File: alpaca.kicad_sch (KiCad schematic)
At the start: 83 parts, among them P1 Debug, P2 Endpoint, U1 Raspberry_Pico, U10 ST_LSM6, U12 ST_LSM6, U2 Alpsalpine_RKJXV, U3 Alpsalpine_EC10E, U4 Alpsalpine_RKJXM, U6 NXP_PCAL6416A, U8 NXP_PCAL6416A

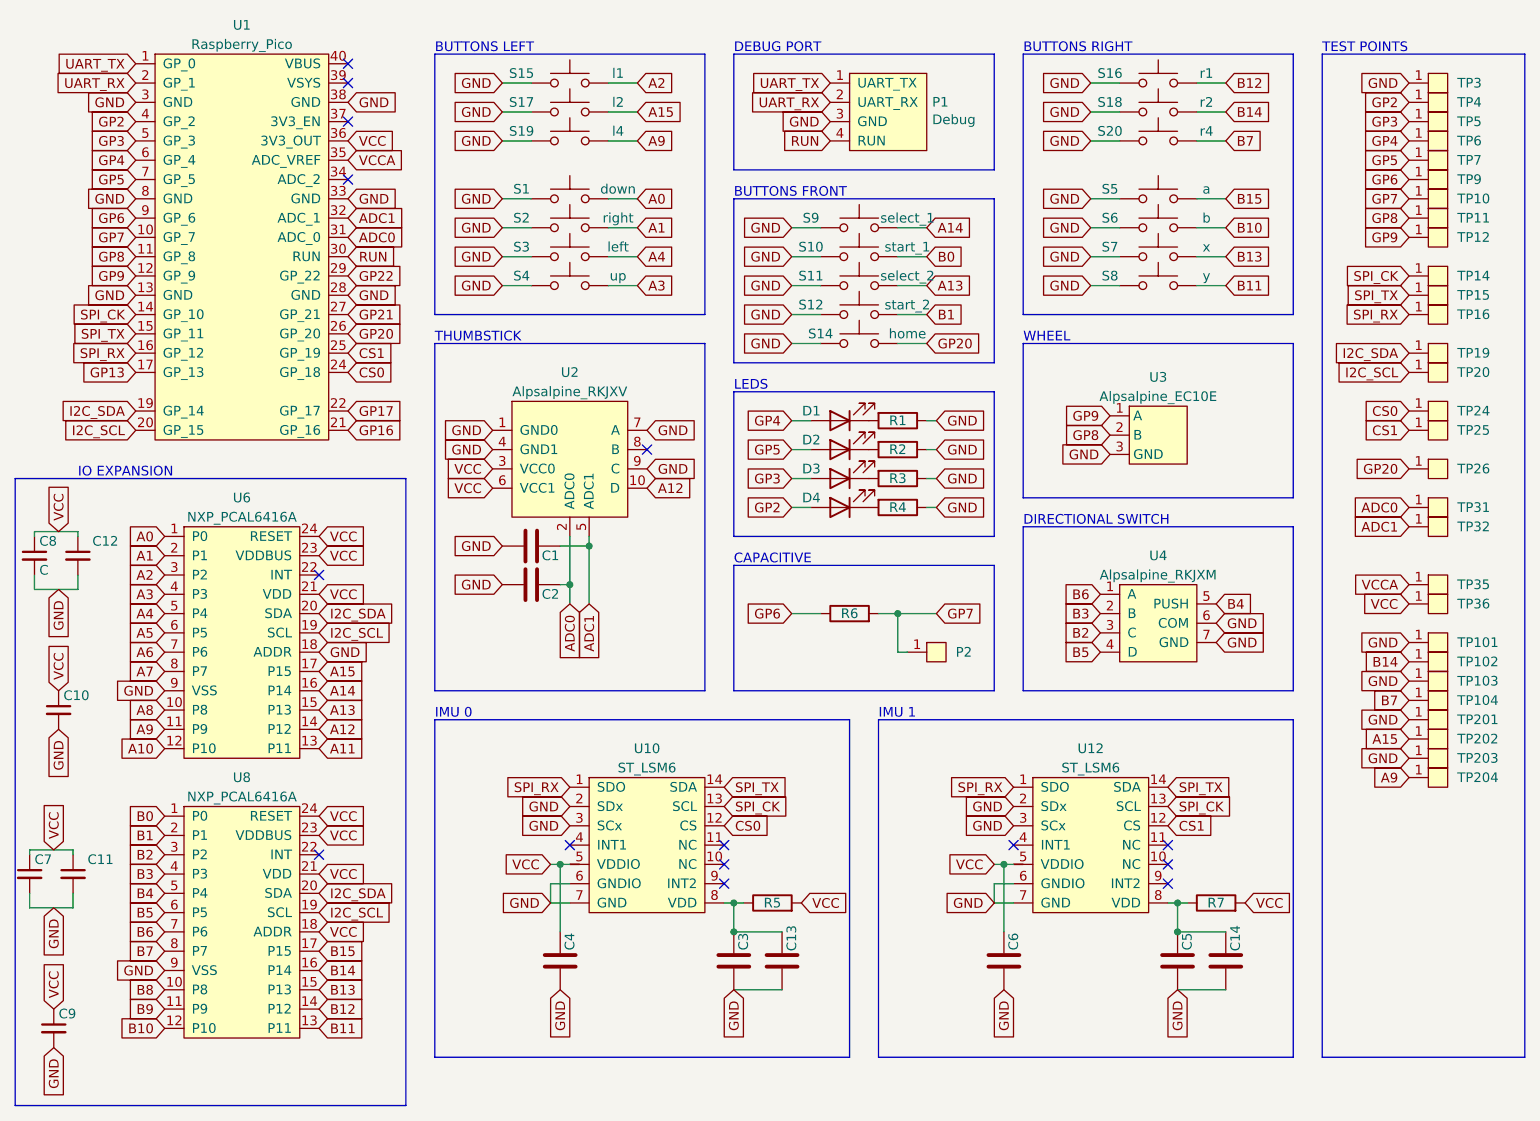
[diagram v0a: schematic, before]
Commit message: Adding hierarchical sheets and bus definitions
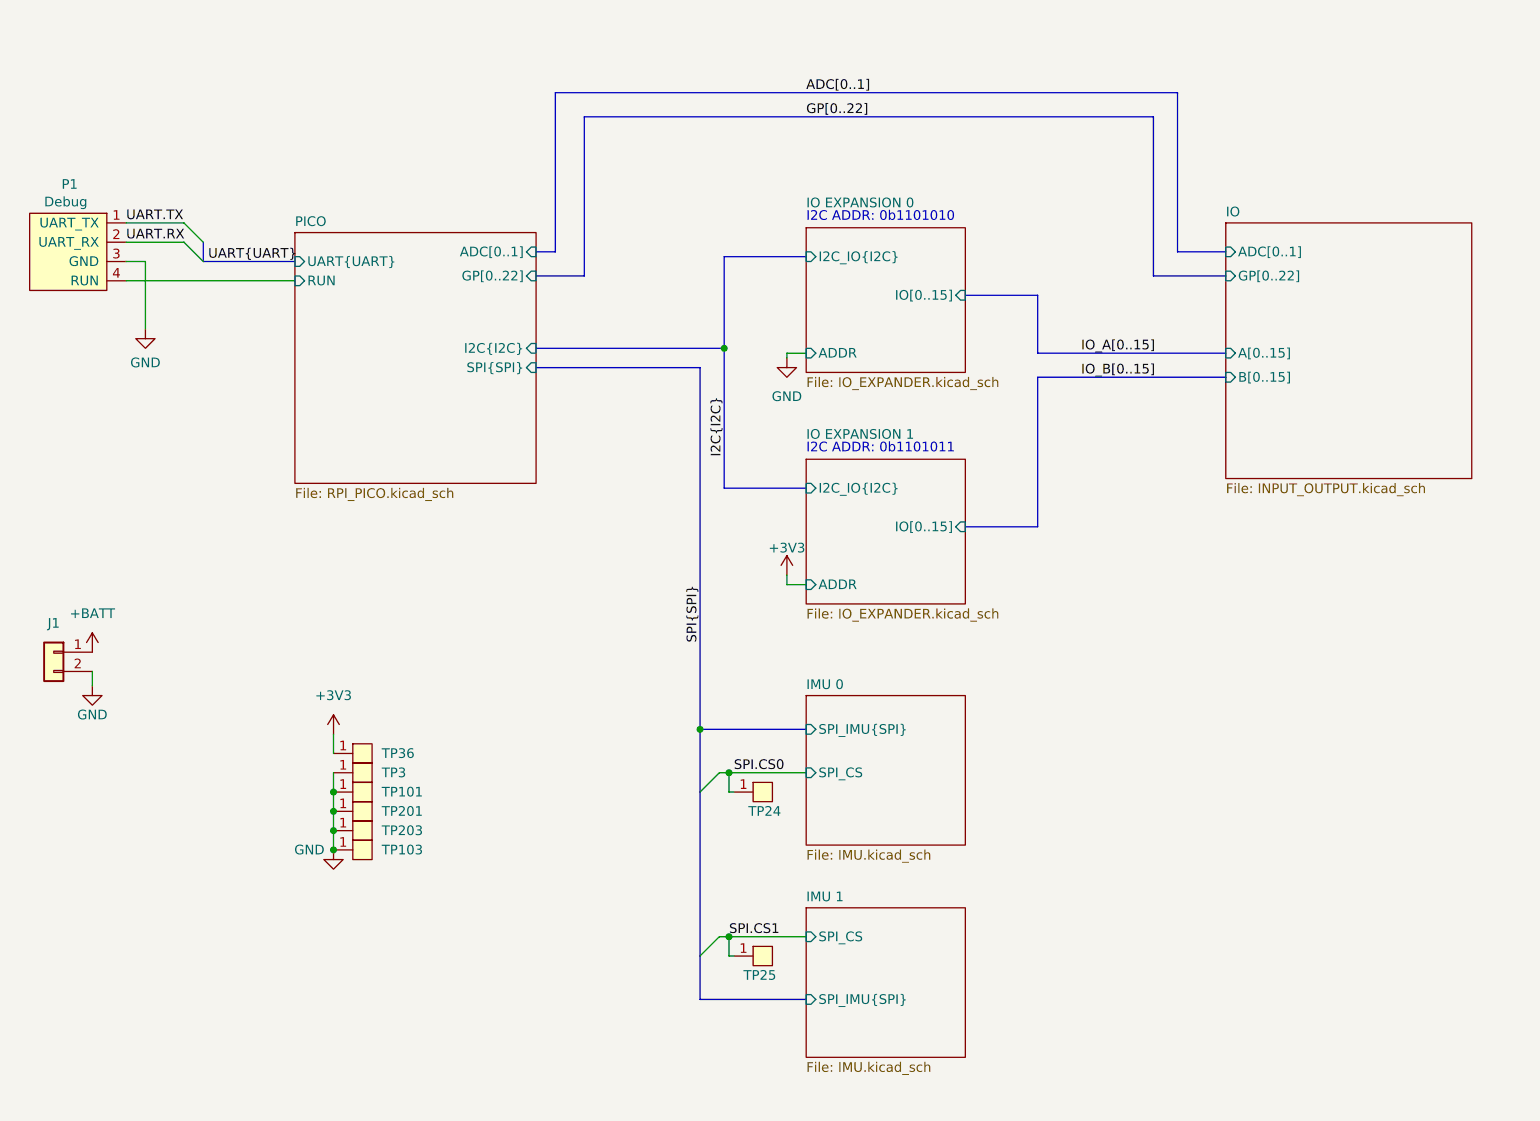
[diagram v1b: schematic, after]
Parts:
- removed C1, C2, C3, C4, C5, C6: C, Capacitor_SMD:C_0402_1005Metric, symbol Device:C
- removed C10, C9: C, Capacitor_SMD:C_0603_1608Metric, symbol Device:C_Small
- removed C11, C12: C, Capacitor_SMD:C_0805_2012Metric, symbol Device:C_Small
- removed C13, C14: C, Capacitor_SMD:C_0603_1608Metric, symbol Device:C
- removed C7, C8: C, Capacitor_SMD:C_0402_1005Metric, symbol Device:C_Small
- removed D1, D2, D3, D4: Diode, ILO_fp:0603_d, symbol Device:LED
- removed P2: Endpoint, ILO_fp:HRO_BC-25-3P, symbol ILO_sym:Endpoint
- removed R1, R2, R3, R4, R5, R7: R, ILO_fp:0603, symbol Device:R
- removed R6: R6, ILO_fp:0402, symbol Device:R
- removed S1: down, ILO_fp:Alpsalpine_SKPM, symbol Switch:SW_Push
- removed S10: start_1, ILO_fp:Alpsalpine_SKPM, symbol Switch:SW_Push
- removed S11: select_2, ILO_fp:Alpsalpine_SKPM, symbol Switch:SW_Push
- removed S12: start_2, ILO_fp:Alpsalpine_SKPM, symbol Switch:SW_Push
- removed S14: home, ILO_fp:Alpsalpine_SKPM, symbol Switch:SW_Push
- removed S15: l1, ILO_fp:Alpsalpine_SKHHL, symbol Switch:SW_Push
- removed S16: r1, ILO_fp:Alpsalpine_SKHHL, symbol Switch:SW_Push
- removed S17: l2, ILO_fp:Alpsalpine_SKQG, symbol Switch:SW_Push
- removed S18: r2, ILO_fp:Alpsalpine_SKQG, symbol Switch:SW_Push
- removed S19: l4, ILO_fp:Alpsalpine_SKQG, symbol Switch:SW_Push
- removed S2: right, ILO_fp:Alpsalpine_SKPM, symbol Switch:SW_Push
- removed S20: r4, ILO_fp:Alpsalpine_SKQG, symbol Switch:SW_Push
- removed S3: left, ILO_fp:Alpsalpine_SKPM, symbol Switch:SW_Push
- removed S4: up, ILO_fp:Alpsalpine_SKPM, symbol Switch:SW_Push
- removed S5: a, ILO_fp:Alpsalpine_SKPM, symbol Switch:SW_Push
- removed S6: b, ILO_fp:Alpsalpine_SKPM, symbol Switch:SW_Push
- removed S7: x, ILO_fp:Alpsalpine_SKPM, symbol Switch:SW_Push
- removed S8: y, ILO_fp:Alpsalpine_SKPM, symbol Switch:SW_Push
- removed S9: select_1, ILO_fp:Alpsalpine_SKPM, symbol Switch:SW_Push
- removed TP10, TP102, TP104, TP11, TP12, TP14, TP15, TP16, TP19, TP20, TP202, TP204, TP26, TP31, TP32, TP35, TP4, TP5, TP6, TP7, TP9: Endpoint, ILO_fp:Pad_1mm, symbol ILO_sym:Endpoint
- removed U1: Raspberry_Pico, ILO_fp:Raspberry_Pico, symbol ILO_sym:Raspberry_Pico
- removed U10, U12: ST_LSM6, ILO_fp:LGA14, symbol ILO_sym:ST_LSM6
- removed U2: Alpsalpine_RKJXV, ILO_fp:Alpsalpine_RKJXV122400R, symbol ILO_sym:Alpsalpine_RKJXV
- removed U3: Alpsalpine_EC10E, ILO_fp:Alpsalpine_EC10E, symbol ILO_sym:Alpsalpine_EC10E
- removed U4: Alpsalpine_RKJXM, ILO_fp:Alpsalpine_RKJXM1015004, symbol ILO_sym:Alpsalpine_RKJXM
- removed U6, U8: NXP_PCAL6416A, ILO_fp:QFN24, symbol ILO_sym:NXP_PCAL6416A
- added J1: Conn_01x02, symbol Connector_Generic:Conn_01x02
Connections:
- net GND: now also J1.2 (Pin_2)
- net CS0 renamed SPI.CS0
- net CS1 renamed SPI.CS1
- net RUN renamed PICO/RUN
- net UART_RX renamed UART.RX
- net UART_TX renamed UART.TX
- net VCC renamed +3V3
- new net +BATT: J1.1 (Pin_1)
- no-connect marks 15 -> 0
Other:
- added sheet IMU 0 (IMU.kicad_sch)
- added sheet IMU 1 (IMU.kicad_sch)
- added sheet IO (INPUT_OUTPUT.kicad_sch)
- added sheet IO EXPANSION 0 (IO_EXPANDER.kicad_sch)
- added sheet IO EXPANSION 1 (IO_EXPANDER.kicad_sch)
- added sheet PICO (RPI_PICO.kicad_sch)
- note added: "I2C ADDR: 0b1101010"
- note added: "I2C ADDR: 0b1101011"
- note removed: "BUTTONS FRONT"
- note removed: "BUTTONS LEFT"
- note removed: "BUTTONS RIGHT"
- note removed: "CAPACITIVE"
- note removed: "DEBUG PORT"
- note removed: "DIRECTIONAL SWITCH"
- note removed: "IMU 0"
- note removed: "IMU 1"
- note removed: "IO EXPANSION"
- note removed: "LEDS"
- note removed: "TEST POINTS"
- note removed: "THUMBSTICK"
- note removed: "WHEEL"
- moved on the sheet: TP101, TP103, TP201, TP203, TP24, TP25, TP3, TP36
